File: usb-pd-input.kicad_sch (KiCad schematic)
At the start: 21 parts, among them J1 USB-C, J2 Pogo pads, J3 Pogo pads (debug), Q1 -30V -4A, U1 STUSB4500QTR

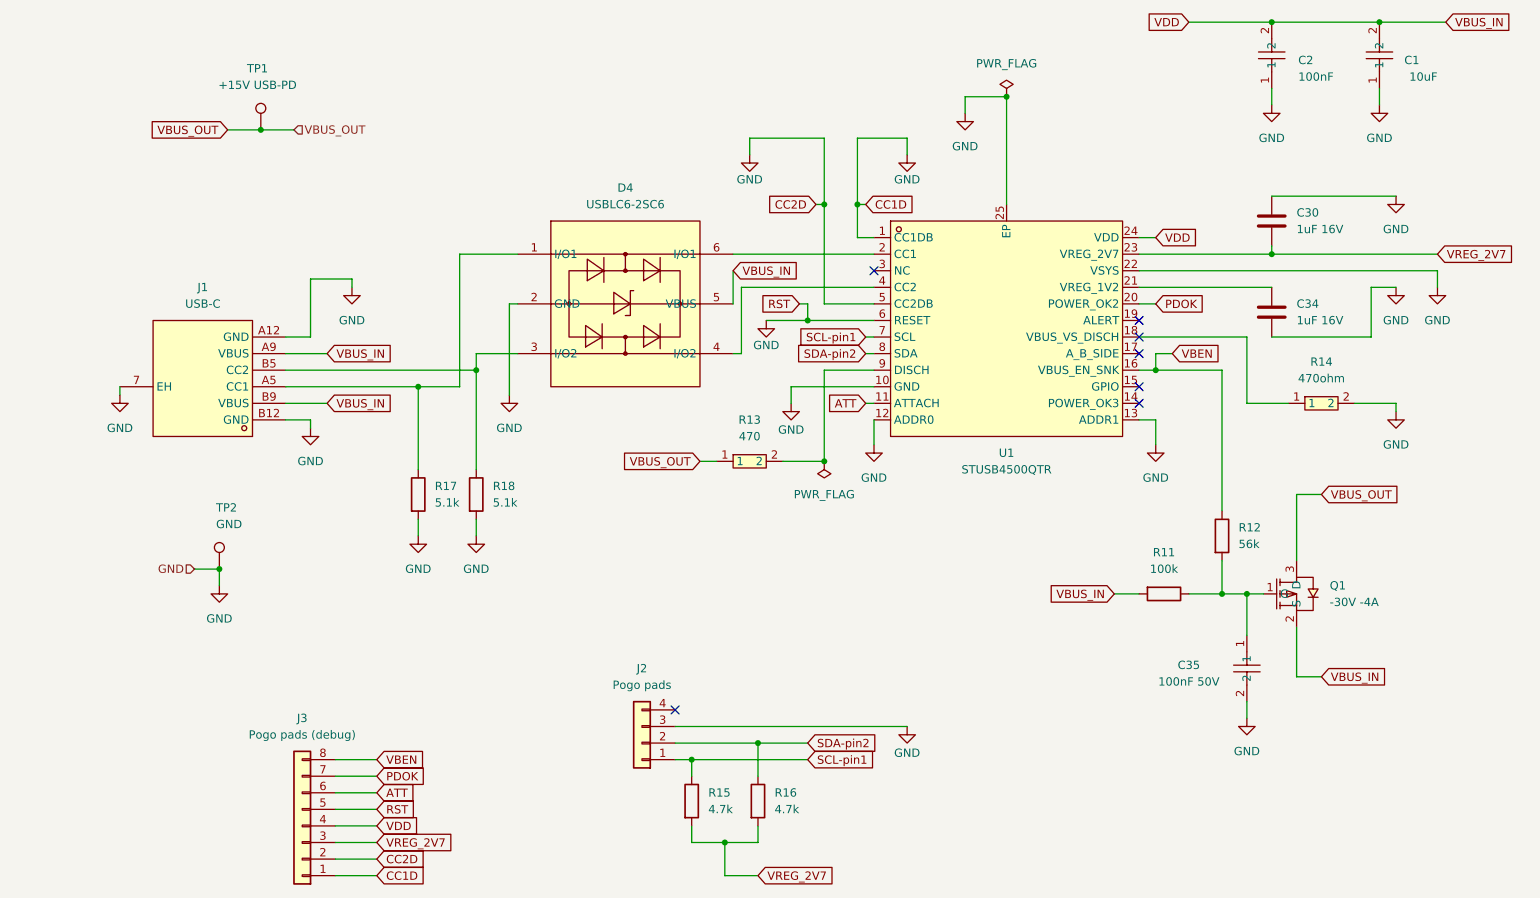
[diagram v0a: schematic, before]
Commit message: feat(usb-pd): add 0 Ω jumpers (R19/R20) on CC1DB/CC2DB → GND for v3 chip isolation & test point resilience
Implements defensive v3 CC pin fix:
- Add R19 (0 Ω, 0603) from STUSB4500 CC1DB pin to GND
- Add R20 (0 Ω, 0603) from STUSB4500 CC2DB pin to GND
- Preserves named `CC1DB`/`CC2DB` nets for J3 pogo probing and future chip-isolation debug
- Net `GND` → `GND rail` for PCB copper pour clarity
- Schematic cleanup: reorganize junctions to reflect actual net topology

Documentation updated to reflect completed implementation steps and test point function.

Co-Authored-By: Claude Opus 4.7 <noreply@anthropic.com>
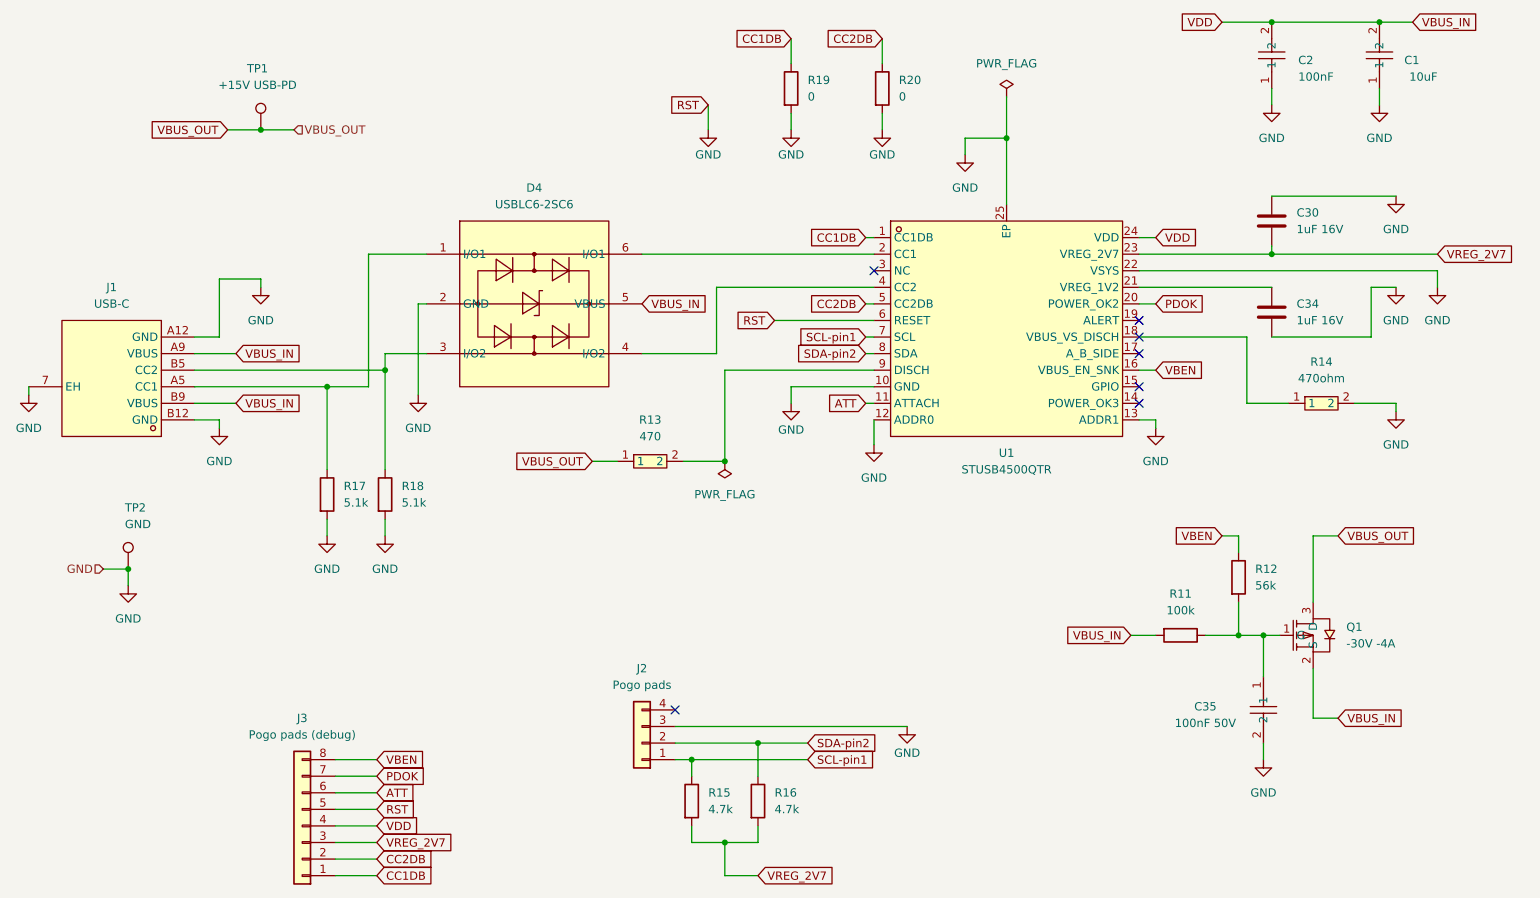
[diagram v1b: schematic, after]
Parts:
- added R19, R20: 0, zudo-pd:R0603, symbol Device:R
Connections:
- net GND: now also R19.2, R20.2; no longer J3.1 (Pin_1), J3.2 (Pin_2), U1.1 (CC1DB), U1.5 (CC2DB)
- new net CC1DB: J3.1 (Pin_1), R19.1, U1.1 (CC1DB)
- new net CC2DB: J3.2 (Pin_2), R20.1, U1.5 (CC2DB)
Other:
- moved on the sheet: C35, D4, J1, Q1, R11, R12, R13, R17, R18, TP2
